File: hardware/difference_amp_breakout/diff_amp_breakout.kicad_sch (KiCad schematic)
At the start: 28 parts, among them J1 VDD, J2 GND, J3 IIN, J4 IOUT, J5 OUT, U1 OPA2356xxD, U3 LM27761

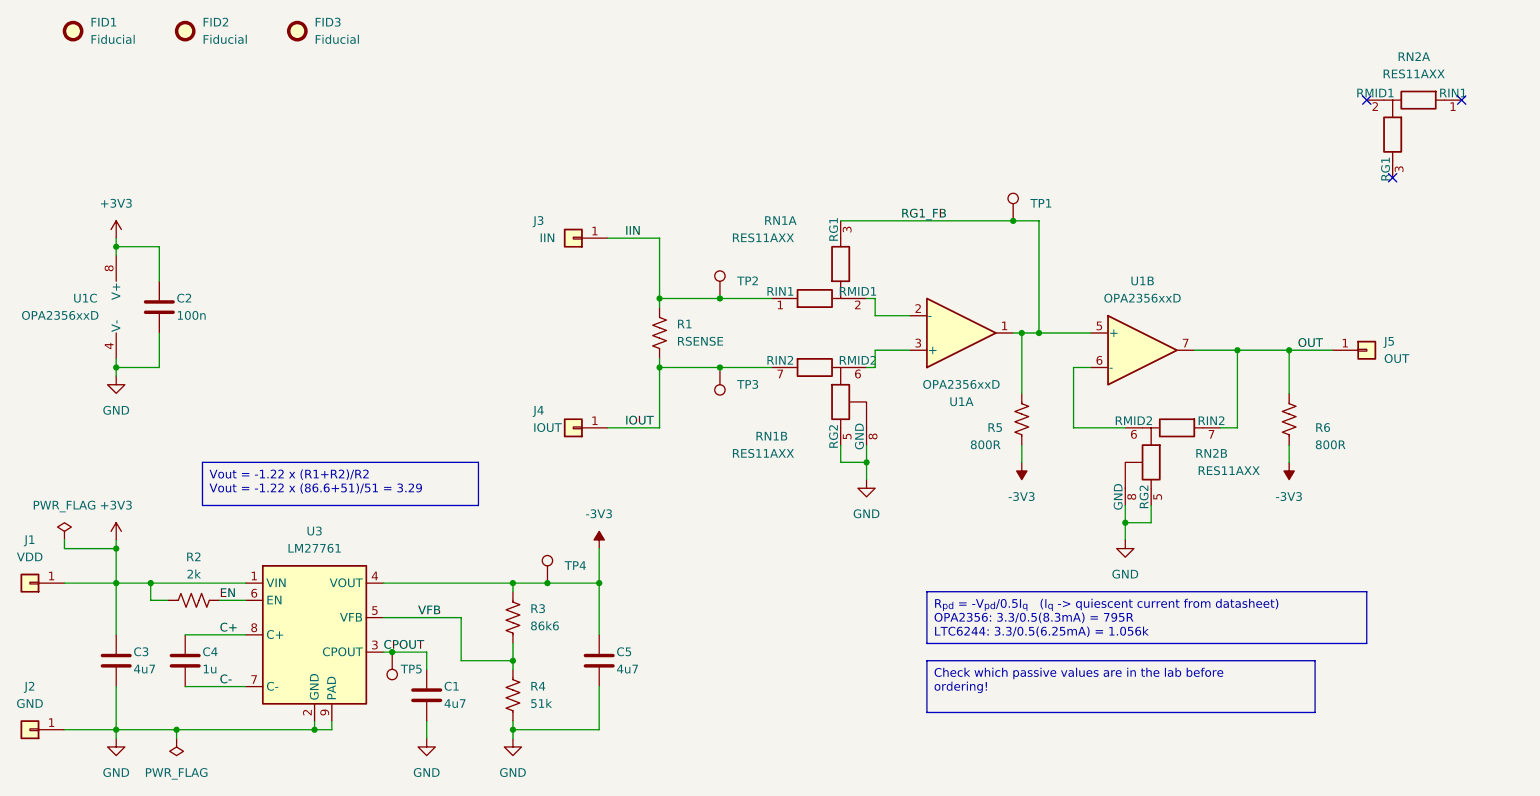
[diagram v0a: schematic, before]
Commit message: Rev C pcb complete, last commit before branching firmware for new board
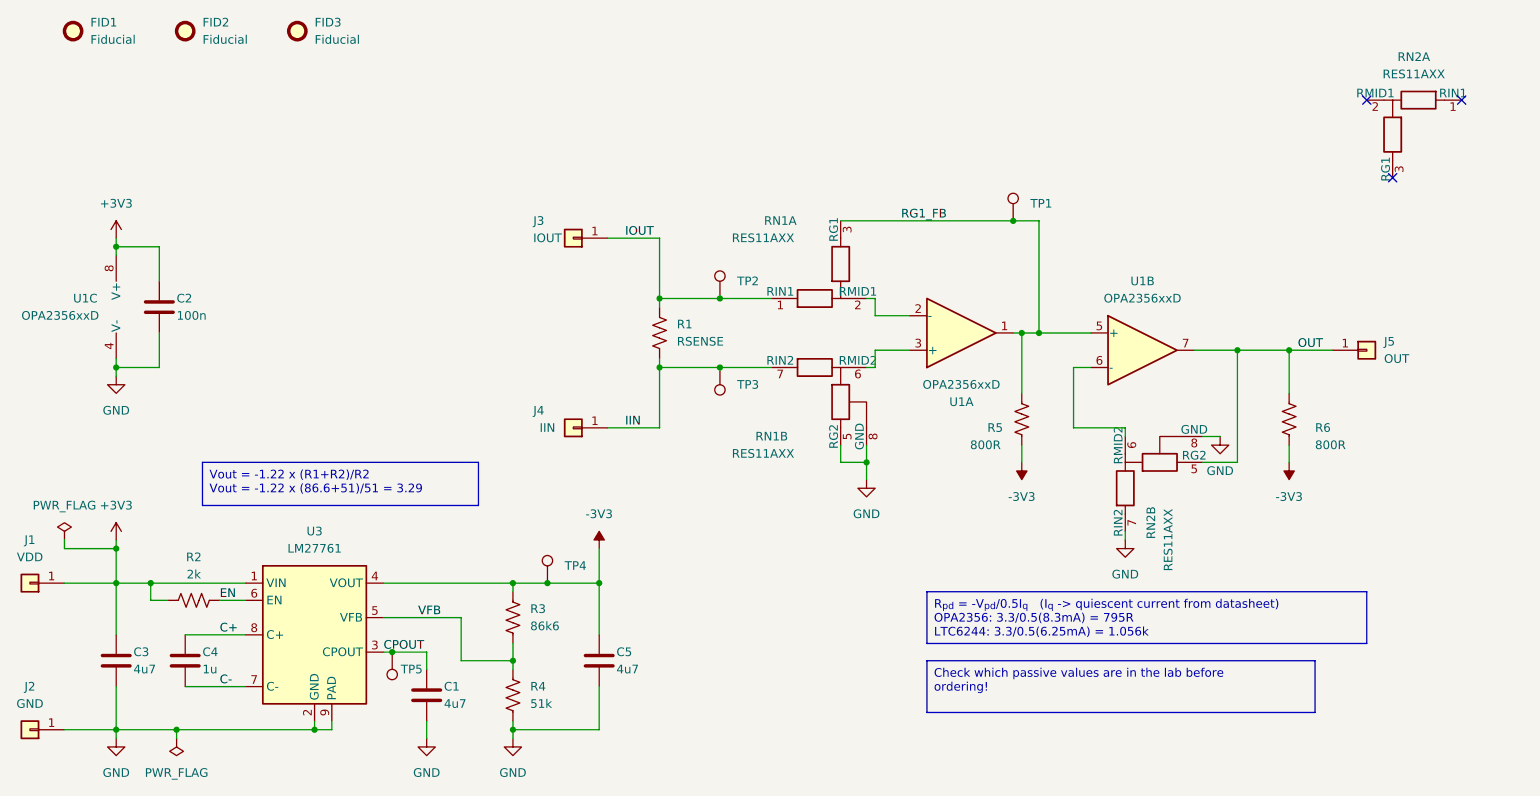
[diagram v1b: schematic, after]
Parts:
- J3: value IIN -> IOUT
- J4: value IOUT -> IIN
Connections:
- net GND: now also RN2.7 (RIN2); no longer RN2.5 (RG2)
- net IIN: now also J4.1 (Pin_1), R1.2, RN1.7 (RIN2), TP3.1; no longer J3.1 (Pin_1), R1.1, RN1.1 (RIN1), TP2.1
- net IOUT: now also J3.1 (Pin_1), R1.1, RN1.1 (RIN1), TP2.1; no longer J4.1 (Pin_1), R1.2, RN1.7 (RIN2), TP3.1
- net OUT: now also RN2.5 (RG2); no longer RN2.7 (RIN2)
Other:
- moved on the sheet: RN2B
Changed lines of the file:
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@@
 	)
 	(junction
+		(at 210.82 93.98)
+		(diameter 0)
+		(color 0 0 0 0)
+	)
+	(junction
 		(at 125.73 86.36)
 		(diameter 0)
@@
 	)
 	(junction
-		(at 210.82 93.98)
-		(diameter 0)
-		(color 0 0 0 0)
-	)
-	(junction
-		(at 194.31 119.38)
-		(diameter 0)
-		(color 0 0 0 0)
-	)
-	(junction
 		(at 218.44 93.98)
 		(diameter 0)
@@
 	(wire
 		(pts
-			(xy 194.31 116.84) (xy 194.31 119.38)
-		)
-		(stroke
-			(width 0)
-			(type default)
-		)
-	)
-	(wire
-		(pts
 			(xy 55.88 135.89) (xy 64.77 135.89)
 		)
@@
 	(wire
 		(pts
-			(xy 194.31 105.41) (xy 186.69 105.41)
-		)
-		(stroke
-			(width 0)
-			(type default)
-		)
-	)
-	(wire
-		(pts
 			(xy 218.44 93.98) (xy 218.44 100.33)
 		)
@@
 	(wire
 		(pts
-			(xy 86.36 138.43) (xy 85.09 138.43)
+			(xy 205.74 106.68) (xy 208.28 106.68)
 		)
 		(stroke
@@
 	(wire
 		(pts
-			(xy 181.61 91.44) (xy 189.23 91.44)
+			(xy 86.36 138.43) (xy 85.09 138.43)
 		)
 		(stroke
@@
 	(wire
 		(pts
-			(xy 179.07 91.44) (xy 179.07 100.33)
+			(xy 181.61 91.44) (xy 189.23 91.44)
 		)
 		(stroke
@@
 	(wire
 		(pts
-			(xy 210.82 93.98) (xy 218.44 93.98)
+			(xy 179.07 91.44) (xy 179.07 100.33)
 		)
 		(stroke
@@
 	(wire
 		(pts
-			(xy 210.82 93.98) (xy 210.82 105.41)
-		)
-		(stroke
-			(width 0)
-			(type default)
-		)
-	)
-	(wire
-		(pts
 			(xy 109.22 128.27) (xy 104.14 128.27)
 		)
@@
 	(wire
 		(pts
-			(xy 194.31 119.38) (xy 194.31 121.92)
+			(xy 45.72 77.47) (xy 45.72 78.74)
 		)
 		(stroke
@@
 	(wire
 		(pts
-			(xy 45.72 77.47) (xy 45.72 78.74)
+			(xy 179.07 91.44) (xy 181.61 91.44)
 		)
 		(stroke
@@
 	(wire
 		(pts
-			(xy 179.07 91.44) (xy 181.61 91.44)
+			(xy 45.72 149.86) (xy 54.61 149.86)
 		)
 		(stroke
@@
 	(wire
 		(pts
-			(xy 45.72 149.86) (xy 54.61 149.86)
+			(xy 179.07 107.95) (xy 179.07 110.49)
 		)
 		(stroke
@@
 	(wire
 		(pts
-			(xy 179.07 107.95) (xy 179.07 110.49)
+			(xy 104.14 137.16) (xy 104.14 139.7)
 		)
 		(stroke
@@
 	(wire
 		(pts
-			(xy 104.14 137.16) (xy 104.14 139.7)
+			(xy 156.21 86.36) (xy 157.48 86.36)
 		)
 		(stroke
@@
 	(wire
 		(pts
-			(xy 156.21 86.36) (xy 157.48 86.36)
+			(xy 205.74 110.49) (xy 210.82 110.49)
 		)
 		(stroke
@@
 	(wire
 		(pts
-			(xy 208.28 105.41) (xy 210.82 105.41)
-		)
-		(stroke
-			(width 0)
-			(type default)
-		)
-	)
-	(wire
-		(pts
 			(xy 142.24 96.52) (xy 134.62 96.52)
 		)
@@
 	(wire
 		(pts
+			(xy 194.31 105.41) (xy 194.31 106.68)
+		)
+		(stroke
+			(width 0)
+			(type default)
+		)
+	)
+	(wire
+		(pts
 			(xy 116.84 149.86) (xy 104.14 149.86)
 		)
@@
 	(wire
 		(pts
-			(xy 198.12 116.84) (xy 198.12 119.38)
+			(xy 210.82 93.98) (xy 218.44 93.98)
 		)
 		(stroke
@@
 	(wire
 		(pts
+			(xy 194.31 120.65) (xy 194.31 121.92)
+		)
+		(stroke
+			(width 0)
+			(type default)
+		)
+	)
+	(wire
+		(pts
 			(xy 85.09 128.27) (xy 104.14 128.27)
 		)
@@
 	(wire
 		(pts
+			(xy 210.82 93.98) (xy 210.82 110.49)
+		)
+		(stroke
+			(width 0)
+			(type default)
+		)
+	)
+	(wire
+		(pts
 			(xy 74.93 149.86) (xy 77.47 149.86)
 		)
@@
 	(wire
 		(pts
-			(xy 198.12 119.38) (xy 194.31 119.38)
+			(xy 186.69 105.41) (xy 194.31 105.41)
 		)
 		(stroke
@@
 		)
 	)
-	(label "IIN"
+	(label "IOUT"
 		(at 120.65 77.47 0)
 		(fields_autoplaced yes)
@@
 		)
 	)
-	(label "IOUT"
+	(label "IIN"
 		(at 120.65 105.41 0)
 		(fields_autoplaced yes)
@@
 			)
 		)
-		(property "Value" "IOUT"
+		(property "Value" "IIN"
 			(at 109.22 105.41 0)
 			(effects
@@
 			)
 		)
-		(property "Value" "IIN"
+		(property "Value" "IOUT"
 			(at 109.22 77.47 0)
 			(effects
@@
 	(symbol
 		(lib_id "DW_Library:RES11AXX")
-		(at 198.12 105.41 0)
-		(mirror y)
+		(at 194.31 110.49 90)
 		(unit 2)
 		(exclude_from_sim no)
@@
 		(dnp no)
 		(property "Reference" "RN2"
-			(at 207.01 109.22 0)
+			(at 198.12 119.38 0)
 			(effects
 				(font
@@
 		)
 		(property "Value" "RES11AXX"
-			(at 209.55 111.76 0)
+			(at 200.66 121.92 0)
 			(effects
 				(font
@@
 		)
 		(property "Footprint" "Package_TO_SOT_SMD:SOT-23-8"
-			(at 207.518 132.588 0)
+			(at 221.488 119.888 0)
 			(effects
 				(font
@@
 		)
 		(property "Datasheet" "https://www.ti.com/lit/ds/symlink/res11a.pdf"
-			(at 204.47 137.16 0)
+			(at 226.06 116.84 0)
 			(effects
 				(font
@@
 		)
 		(property "Description" " 0.05% Matched, Thin-Film Resistor Dividers With 1-kΩ Inputs"
-			(at 198.12 134.62 0)
+			(at 223.52 110.49 0)
 			(effects
 				(font
@@
 				)
 			)
+		)
+	)
+	(symbol
+		(lib_id "power:GND")
+		(at 208.28 106.68 0)
+		(unit 1)
+		(exclude_from_sim no)
+		(in_bom yes)
+		(on_board yes)
+		(dnp no)
+		(property "Reference" "#PWR012"
+			(at 208.28 113.03 0)
+			(effects
+				(font
+					(size 1.27 1.27)
+				)
+				(hide yes)
+			)
+		)
+		(property "Value" "GND"
+			(at 208.28 111.76 0)
+			(effects
+				(font
+					(size 1.27 1.27)
+				)
+			)
+		)
+		(property "Footprint" ""
+			(at 208.28 106.68 0)
+			(effects
+				(font
+					(size 1.27 1.27)
+				)
+				(hide yes)
+			)
+		)
+		(property "Datasheet" ""
+			(at 208.28 106.68 0)
+			(effects
+				(font
+					(size 1.27 1.27)
+				)
+				(hide yes)
+			)
+		)
+		(property "Description" "Power symbol creates a global label with name \"GND\" , ground"
+			(at 208.28 106.68 0)
+			(effects
+				(font
+					(size 1.27 1.27)
+				)
+				(hide yes)
+			)
+		)
+		(pin "1"
+		)
+		(instances
+			(project "diff_amp_breakout"
+				(path "/f66874eb-7661-466c-b72b-2d456792f555"
+					(reference "#PWR012")
+					(unit 1)
+				)
+			)
